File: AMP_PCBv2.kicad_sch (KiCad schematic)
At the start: 111 parts, among them J1 POWER, J2 EBRAKE, J3 MC, J4 STEERING, J5 OLED Breakout, J6 EBRAKE_BREAKOUT, Q1 Q_NMOS_GDS, Q2 Q_NMOS_GDS, Q3 Q_NMOS_GDS, Q4 Q_NMOS_GDS, U1 Teensy4.0, U10 RFM9x, U2 FT234XD, U3 LM1117-ADJ, U4 LM1117-ADJ, U5 74HC157, U6 74HC157, U7 74HC4060, U8 74HC00, U9 TLV272

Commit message: Route new PCB (with LoRa)
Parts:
- removed R20, R21: 10K, Resistor_SMD:R_0805_2012Metric_Pad1.20x1.40mm_HandSolder, symbol Device:R_Small_US
- added H1, H2, H3, H4: MountingHole, MountingHole:MountingHole_3.2mm_M3, symbol Mechanical:MountingHole
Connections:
- net OUT_Steering is gone; now on net STEERING_INPUT_B+: Q4.2 (D), R30.1
- net +12V: no longer C14.1, C15.1, U5.16 (VCC), U6.16 (VCC)
- net +3V3: now also C14.1, C15.1, U5.16 (VCC), U6.16 (VCC)
- net EBRAKE_EN: now also JT3.6 (Pin_6), U1.25 (18_A4_SDA0); no longer JT3.8 (Pin_8), U1.27 (20_A6_TX5_LRCLK1)
- net EBRAKE_IS1: now also JT3.7 (Pin_7), U1.26 (19_A5_SCL0); no longer JT3.9 (Pin_9), U1.28 (21_A7_RX5_BCLK1)
- net EBRAKE_IS2: now also JT3.8 (Pin_8), U1.27 (20_A6_TX5_LRCLK1); no longer JT3.10 (Pin_10), U1.29 (22_A8_CTX1)
- net ERR_EBRAKE1: now also JP8.2 (C), U6.6 (I1b); no longer JP9.2 (C), U6.10 (I1c)
- net ERR_EBRAKE2: now also JP9.2 (C), U6.10 (I1c); no longer JP10.2 (C), U6.13 (I1d)
- net ERR_STEERING: now also JP10.2 (C), U6.13 (I1d); no longer JP8.2 (C), U6.6 (I1b)
- net GND: no longer U3.1 (ADJ), U4.1 (ADJ)
- net LORA_INT: now also JT1.10 (Pin_10), U1.10 (8_TX2_IN1)
- net LORA_RST: now also JT1.11 (Pin_11), U1.11 (9_OUT1C)
- net MCU_EBRAKE1: now also JT1.7 (Pin_7), U1.7 (5_IN2), U6.5 (I0b); no longer JT1.10 (Pin_10), U1.10 (8_TX2_IN1), U6.11 (I0c)
- net MCU_EBRAKE2: now also JT1.8 (Pin_8), U1.8 (6_OUT1D), U6.11 (I0c); no longer JT1.11 (Pin_11), U1.11 (9_OUT1C), U6.14 (I0d)
- net MCU_FB: now also JT1.6 (Pin_6), U1.6 (4_BCLK2); no longer JT1.8 (Pin_8), U1.8 (6_OUT1D)
- net MCU_FS1: now also JT1.2 (Pin_2), U1.2 (0_RX1_CRX2_CS1); no longer JT1.4 (Pin_4), U1.4 (2_OUT2)
- net MCU_FWD: now also JT1.3 (Pin_3), U1.3 (1_TX1_CTX2_MISO1); no longer JT1.5 (Pin_5), U1.5 (3_LRCLK2)
- net MCU_REV: now also JT1.4 (Pin_4), U1.4 (2_OUT2); no longer JT1.6 (Pin_6), U1.6 (4_BCLK2)
- net MCU_STEERING: now also U6.14 (I0d); no longer U6.5 (I0b)
- net MCU_THROTTLE: now also JT1.5 (Pin_5), U1.5 (3_LRCLK2); no longer JT1.7 (Pin_7), U1.7 (5_IN2)
- net MUX_EBRAKE1: now also U6.7 (Zb); no longer U6.9 (Zc)
- net MUX_EBRAKE2: now also U6.9 (Zc); no longer U6.12 (Zd)
- net MUX_FB: no longer J3.5 (Pin_5)
- net MUX_FS1: no longer J3.1 (Pin_1), JX1.4 (Pin_4)
- net MUX_FWD: no longer J3.2 (Pin_2), JX1.3 (Pin_3)
- net MUX_REV: no longer J3.3 (Pin_3), JX1.2 (Pin_2)
- net MUX_STEERING: now also U6.12 (Zd); no longer U6.7 (Zb)
- net MUX_THROTTLE: no longer J3.4 (Pin_4), JX1.1 (Pin_1)
- net OLED_SCL: now also JT3.5 (Pin_5), U1.24 (17_A3_TX4_SDA1); no longer JT3.7 (Pin_7), U1.26 (19_A5_SCL0)
- net OLED_SDA: now also JT3.4 (Pin_4), U1.23 (16_A2_RX4_SCL1); no longer JT3.6 (Pin_6), U1.25 (18_A4_SDA0)
- net OUT_FB: now also J3.5 (Pin_5)
- net OUT_FS1: now also J3.1 (Pin_1), JX1.4 (Pin_4)
- net OUT_FWD: now also J3.2 (Pin_2), JX1.3 (Pin_3)
- net OUT_REV: now also J3.3 (Pin_3), JX1.2 (Pin_2)
- net OUT_THROTTLE: now also J3.4 (Pin_4), JX1.1 (Pin_1)
- net WD_RESET: now also JT3.11 (Pin_11), U1.30 (23_A9_CRX1_MCLK1); no longer JT3.3 (Pin_3), U1.22 (15_A1_RX3_SPDIF_IN)
- net WD_SET: now also JT3.10 (Pin_10), U1.29 (22_A8_CTX1); no longer JT3.2 (Pin_2), U1.21 (14_A0_TX3_SPDIF_OUT)
- net at R3.2, R5.2: now also U3.1 (ADJ)
- net at R4.2, R6.2: now also U4.1 (ADJ)
- removed net RX1: JT1.2 (Pin_2), U1.2 (0_RX1_CRX2_CS1), U2.7 (TXD)
- removed net TX1: JT1.3 (Pin_3), U1.3 (1_TX1_CTX2_MISO1), U2.10 (RXD)
- new net: JT3.9 (Pin_9), U1.28 (21_A7_RX5_BCLK1)
- new net USB_UART_RX: JT3.3 (Pin_3), U1.22 (15_A1_RX3_SPDIF_IN), U2.7 (TXD)
- new net USB_UART_TX: JT3.2 (Pin_2), U1.21 (14_A0_TX3_SPDIF_OUT), U2.10 (RXD)
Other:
- note added: "MOUNTING HOLES"
- moved on the sheet: R3, R4

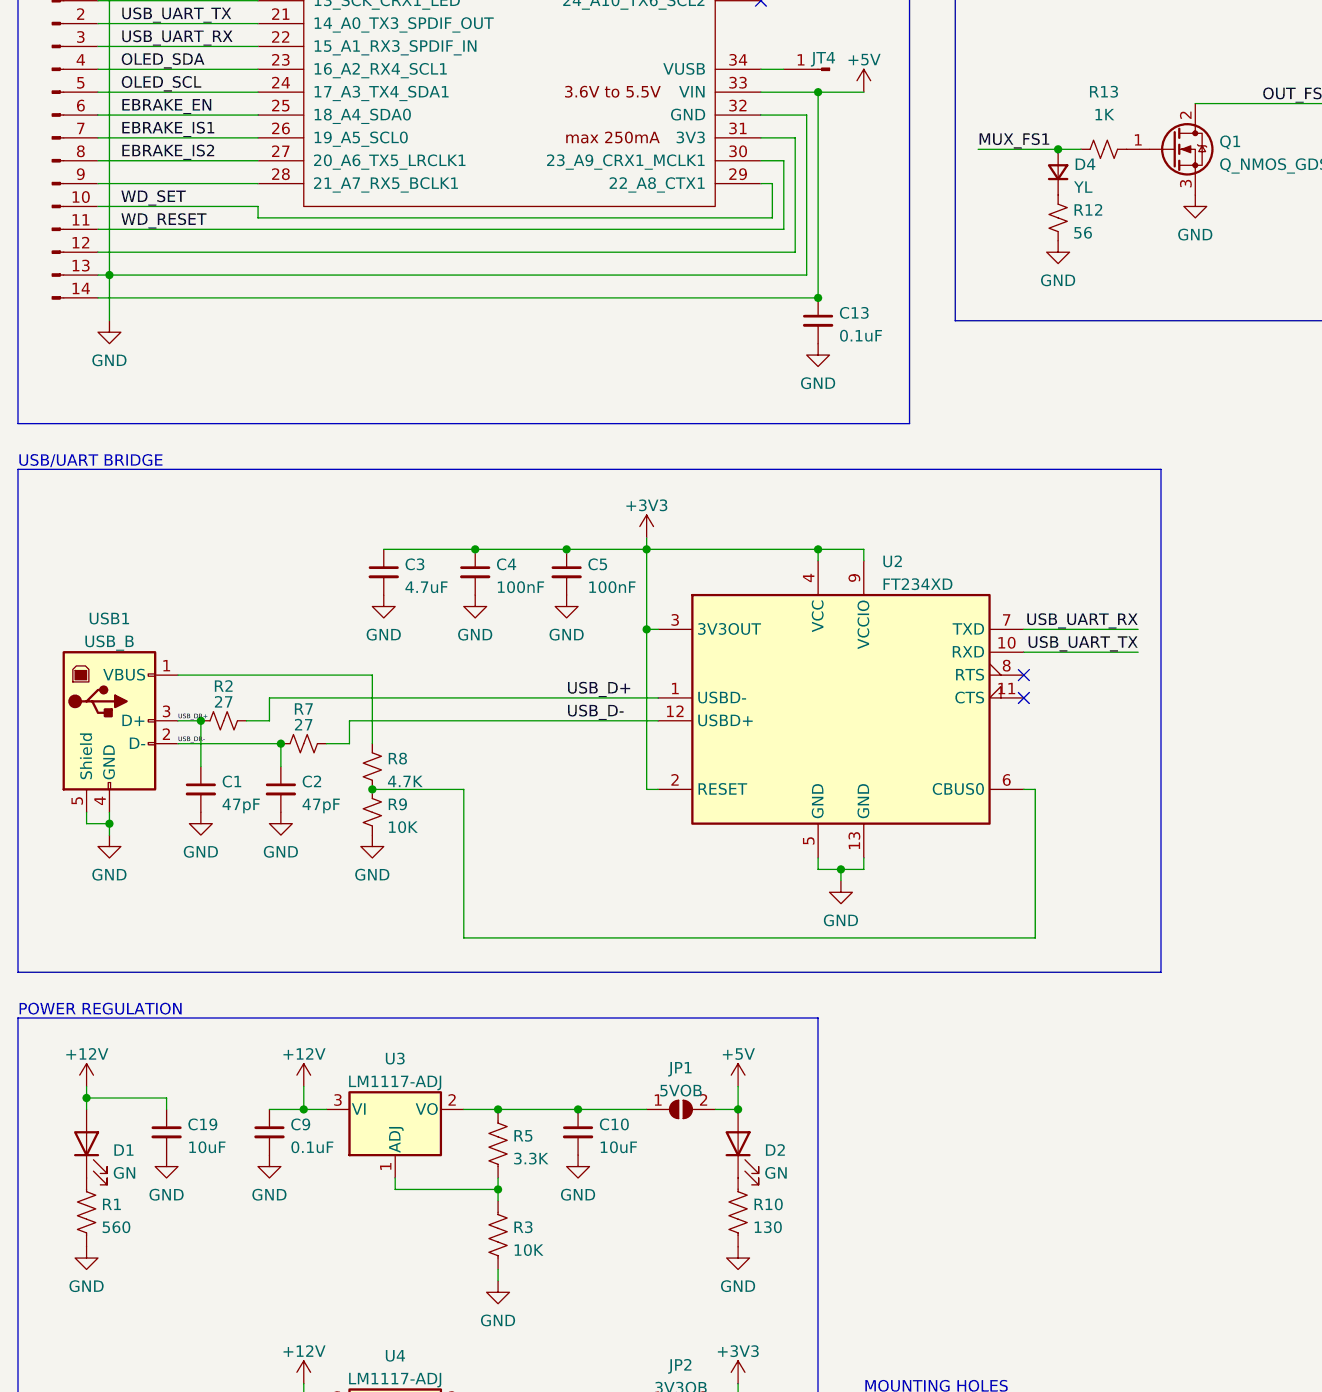
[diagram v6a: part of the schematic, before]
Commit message: Add extra error LED
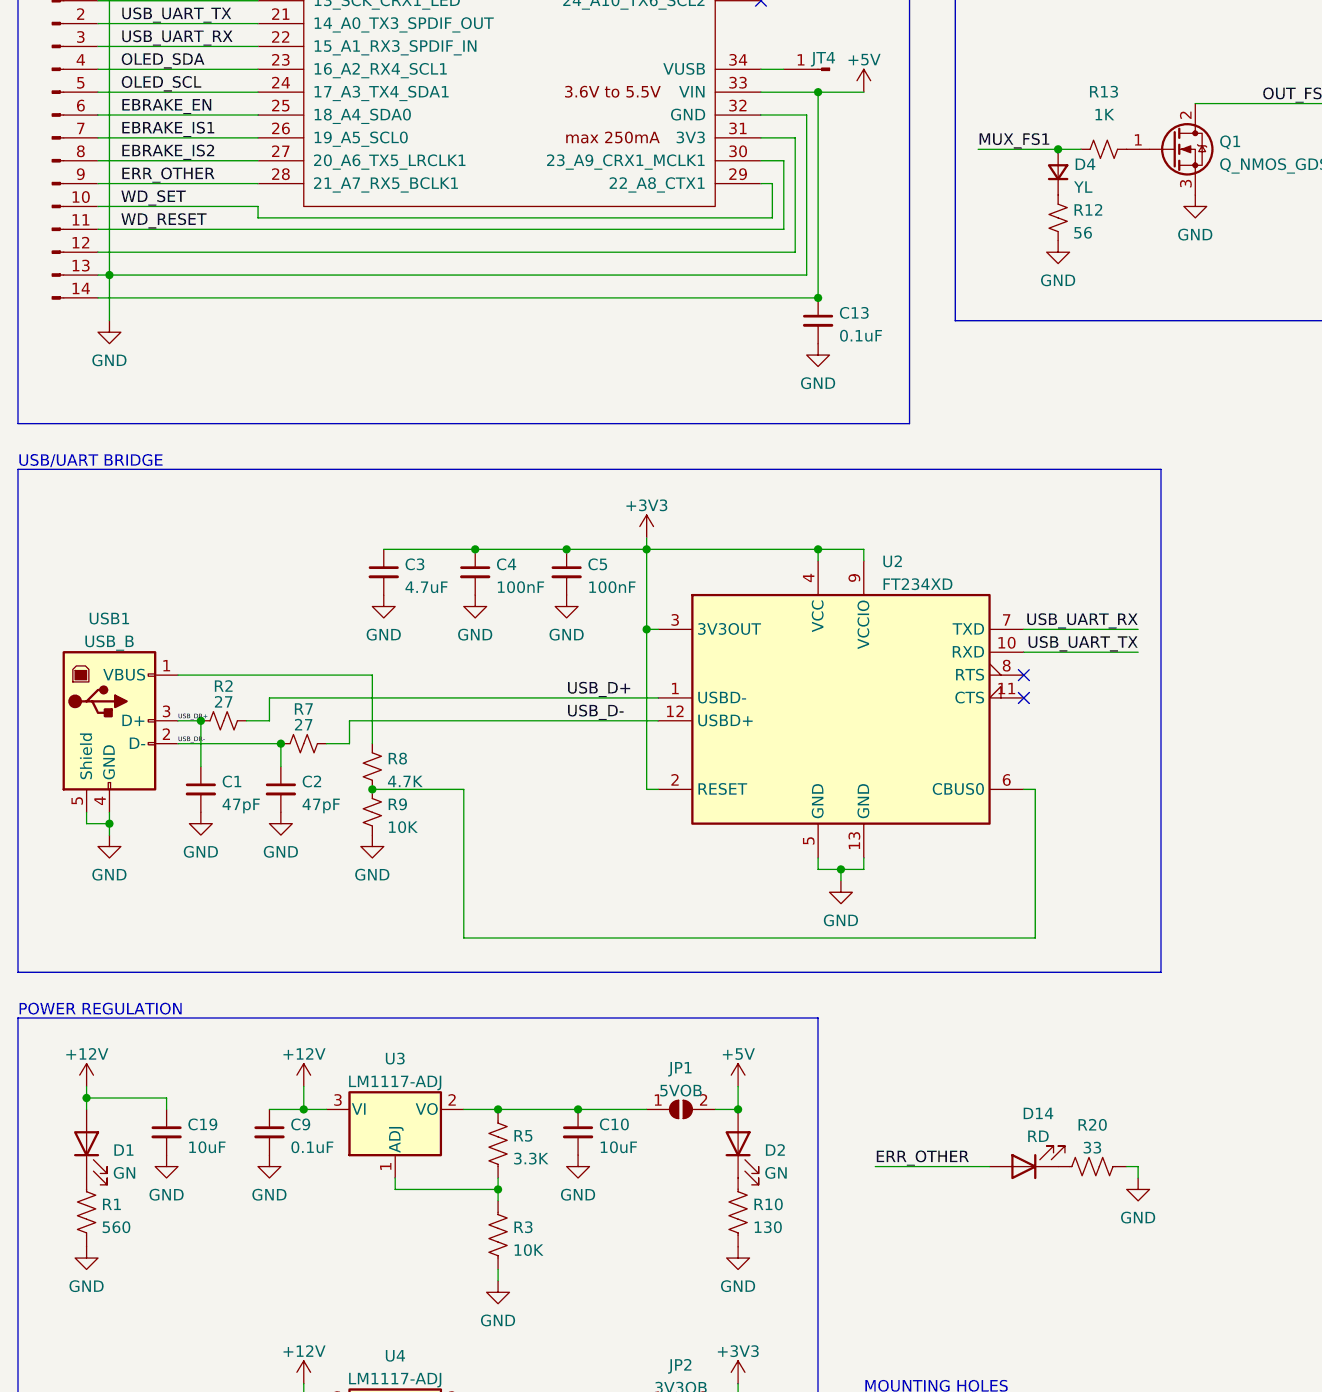
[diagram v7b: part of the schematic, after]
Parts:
- added D14: RD, LED_THT:LED_D5.0mm, symbol Device:LED
- added R20: 33, Resistor_SMD:R_0805_2012Metric_Pad1.20x1.40mm_HandSolder, symbol Device:R_US
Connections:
- net GND: now also R20.2
- net ERR_OTHER: now reaches JT3.9 (Pin_9), U1.28 (21_A7_RX5_BCLK1)
- net ERR_OTHER: now also D14.2 (A)
- new net: D14.1 (K), R20.1
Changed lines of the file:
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@@
     (stroke (width 0) (type default) (color 0 0 0 0))
   )
+  (wire (pts (xy 142.24 204.47) (xy 140.97 204.47))
+    (stroke (width 0) (type default) (color 0 0 0 0))
+  )
   (wire (pts (xy 35.56 149.86) (xy 57.15 149.86))
     (stroke (width 0) (type default) (color 0 0 0 0))
@@
     (stroke (width 0) (type default) (color 0 0 0 0))
   )
+  (wire (pts (xy 113.03 204.47) (xy 125.73 204.47))
+    (stroke (width 0) (type default) (color 0 0 0 0))
+  )
   (wire (pts (xy 328.93 31.75) (xy 328.93 29.21))
     (stroke (width 0) (type default) (color 0 0 0 0))
@@
     (stroke (width 0) (type default) (color 0 0 0 0))
   )
+  (wire (pts (xy 142.24 205.74) (xy 142.24 204.47))
+    (stroke (width 0) (type default) (color 0 0 0 0))
+  )
   (wire (pts (xy 54.61 154.94) (xy 88.9 154.94))
     (stroke (width 0) (type default) (color 0 0 0 0))
@@
     (effects (font (size 1.27 1.27)) (justify right bottom))
   )
+  (label "ERR_OTHER" (at 29.21 95.25 0)
+    (effects (font (size 1.27 1.27)) (justify left bottom))
+  )
   (label "OLED_SDA" (at 379.73 59.69 0)
     (effects (font (size 1.27 1.27)) (justify left bottom))
@@
     (effects (font (size 1.27 1.27)) (justify right bottom))
   )
+  (label "ERR_OTHER" (at 113.03 204.47 0)
+    (effects (font (size 1.27 1.27)) (justify left bottom))
+  )
   (label "OUT_EBRAKE2" (at 349.25 137.16 0)
     (effects (font (size 1.27 1.27)) (justify left bottom))
@@
     (pin "9")
   )
+  (symbol (lib_name "GND_2") (lib_id "power:GND") (at 142.24 205.74 0) (unit 1)
+    (in_bom yes) (on_board yes) (fields_autoplaced)
+    (property "Reference" "#PWR016" (id 0) (at 142.24 212.09 0)
+      (effects (font (size 1.27 1.27)) hide)
+    )
+    (property "Value" "GND" (id 1) (at 142.24 210.1834 0))
+    (property "Footprint" "" (id 2) (at 142.24 205.74 0)
+      (effects (font (size 1.27 1.27)) hide)
+    )
+    (property "Datasheet" "" (id 3) (at 142.24 205.74 0)
+      (effects (font (size 1.27 1.27)) hide)
+    )
+    (pin "1")
+  )
   (symbol (lib_id "Mechanical:MountingHole") (at 115.57 246.38 0) (unit 1)
     (in_bom yes) (on_board yes) (fields_autoplaced)
@@
     (pin "1")
   )
+  (symbol (lib_id "Device:LED") (at 129.54 204.47 180) (unit 1)
+    (in_bom yes) (on_board yes) (fields_autoplaced)
+    (property "Reference" "D14" (id 0) (at 131.1275 198.6112 0))
+    (property "Value" "RD" (id 1) (at 131.1275 201.1481 0))
+    (property "Footprint" "LED_THT:LED_D5.0mm" (id 2) (at 129.54 204.47 0)
+      (effects (font (size 1.27 1.27)) hide)
+    )
+    (property "Datasheet" "~" (id 3) (at 129.54 204.47 0)
+      (effects (font (size 1.27 1.27)) hide)
+    )
+    (pin "1")
+    (pin "2")
+  )
   (symbol (lib_id "power:GND") (at 331.47 83.82 0) (unit 1)
     (in_bom yes) (on_board yes) (fields_autoplaced)
@@
     (pin "2")
   )
+  (symbol (lib_id "Device:R_US") (at 137.16 204.47 90) (unit 1)
+    (in_bom yes) (on_board yes) (fields_autoplaced)
+    (property "Reference" "R20" (id 0) (at 137.16 199.8812 90))
+    (property "Value" "33" (id 1) (at 137.16 202.4181 90))
+    (property "Footprint" "Resistor_SMD:R_0805_2012Metric_Pad1.20x1.40mm_HandSolder" (id 2) (at 137.414 203.454 90)
+      (effects (font (size 1.27 1.27)) hide)
+    )
+    (property "Datasheet" "~" (id 3) (at 137.16 204.47 0)
+      (effects (font (size 1.27 1.27)) hide)
+    )
+    (pin "1")
+    (pin "2")
+  )
   (symbol (lib_id "power:+12V") (at 271.78 34.29 0) (unit 1)
     (in_bom yes) (on_board yes) (fields_autoplaced)
@@
       (reference "#PWR015") (unit 1) (value "GND") (footprint "")
     )
+    (path "/2d6f3053-ade8-4f48-9f13-1744b40222da"
+      (reference "#PWR016") (unit 1) (value "GND") (footprint "")
+    )
     (path "/7cfae825-7739-4de8-81a2-731760c0c369"
       (reference "#PWR0101") (unit 1) (value "GND") (footprint "")
@@
       (reference "D13") (unit 1) (value "RD") (footprint "LED_THT:LED_D5.0mm")
     )
+    (path "/7cab1306-be44-4b98-bea8-a9e11091e37d"
+      (reference "D14") (unit 1) (value "RD") (footprint "LED_THT:LED_D5.0mm")
+    )
     (path "/c4aadec5-42db-4fad-a3f8-5eb8777cba6d"
       (reference "H1") (unit 1) (value "MountingHole") (footprint "MountingHole:MountingHole_3.2mm_M3")
@@
       (reference "R19") (unit 1) (value "1.8K") (footprint "Resistor_SMD:R_0805_2012Metric_Pad1.20x1.40mm_HandSolder")
     )
+    (path "/89e6758b-0753-4670-9f9f-c0620d52cba3"
+      (reference "R20") (unit 1) (value "33") (footprint "Resistor_SMD:R_0805_2012Metric_Pad1.20x1.40mm_HandSolder")
+    )
     (path "/dbe172b2-9008-4550-9208-59697ad822e3"
